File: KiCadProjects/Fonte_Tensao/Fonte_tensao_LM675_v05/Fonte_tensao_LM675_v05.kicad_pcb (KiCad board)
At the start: 2 copper layers, 90 x 100 mm, 33 parts, among them J1 alimentacao analogica, J2 sinais analogicos, J3 comunicacao / sinais digitais, J4 Barrel_Jack, U1 L7809, U2 LM7909_TO220, U3 LM675, U4 L7805, U5 L7905, U6 LM1117T-3.3

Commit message: Roteamento PCB v05
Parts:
- moved C8 95.9 mm to (119.8, 142.2)
- moved C9 87.9 mm to (125.5, 142.2)
- moved U6 76.9 mm to (127.5, 146.8), turned to 180 degrees
- moved U3 75.6 mm to (172.6, 141.6), turned to 180 degrees
- moved C5 74.6 mm to (166.8, 123.5)
- moved SW_kcd1 65.1 mm to (140.3, 83.1)
- moved green1 63.5 mm to (141.3, 145.5)
- moved red1 63.5 mm to (148.8, 145.5)
- moved R1 60.3 mm to (151.5, 122.7), turned to -90 degrees
- moved R2 50.1 mm to (143.8, 117.7), turned to -90 degrees
- moved U5 44.9 mm to (172.4, 55.0)
- moved R6 44.2 mm to (172.7, 111.8), turned to 90 degrees
- moved D1 38.6 mm to (110.9, 67.2)
- moved R7 35.3 mm to (160.0, 115.9), turned to -90 degrees
- moved U2 31.6 mm to (159.9, 55.0)
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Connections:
- J3 pad 16: GND -> Earth
- J3 pad 22: GND -> Earth
- J3 pad 25: GND -> Earth
- J3 pad 28: GND -> Earth
- J3 pad 3: GND -> Earth
- J3 pad 31: GND -> Earth
- J3 pad 34: GND -> Earth
- J3 pad 4: GND -> Earth
- J3 pad 6: GND -> Earth
- J3 pad 7: GND -> Earth
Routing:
- net Earth: track 5.08 -> 437.1 mm
- net VEE: track 0.00 -> 236.0 mm, vias 0 -> 2
- net VCC: track 0.00 -> 174.1 mm
- net +3.3V: track 0.00 -> 104.9 mm
- net Net-(U3-+): track 0.00 -> 94.5 mm
- net -9V: track 0.00 -> 90.0 mm
- net +5V: track 0.00 -> 71.1 mm
- net Net-(U3--): track 0.00 -> 66.6 mm
- net +9V: track 0.00 -> 47.6 mm
- net Net-(green1-A): track 0.00 -> 20.2 mm
- net -5V: track 0.00 -> 18.2 mm
- net Net-(red1-A): track 0.00 -> 15.2 mm
- net Net-(J4-Pad1): track 0.00 -> 12.2 mm
- net Net-(C5-Pad1): track 0.00 -> 6.77 mm
- net GND: track 5.08 -> 0.00 mm
- added copper zone on B.Cu, net Earth

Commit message: placa fonte tensao roteada
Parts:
- moved R6 67.3 mm to (113.2, 143.3)
- moved R5 47.3 mm to (116.2, 123.9), turned to -90 degrees
- moved U3 46.4 mm to (126.2, 141.6)
- moved C9 45.3 mm to (170.8, 142.1)
- moved C8 45.3 mm to (165.0, 142.1)
- moved U6 45.3 mm to (172.8, 146.6)
- moved R1 9.96 mm to (143.8, 116.4)
- moved R2 9.22 mm to (151.5, 122.7)
- moved green1 7.70 mm to (149.0, 145.5)
- moved red1 7.50 mm to (141.3, 145.5)
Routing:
- net Net-(U3--): track 66.6 -> 28.5 mm
- net +3.3V: track 104.9 -> 87.0 mm
- net VEE: track 236.0 -> 252.2 mm, vias 2 -> 1
- net VCC: track 174.1 -> 185.7 mm
- net Earth: track 437.1 -> 447.4 mm
- net Net-(U3-+): track 94.5 -> 84.4 mm
- net Net-(red1-A): track 15.2 -> 21.4 mm
- net Net-(green1-A): track 20.2 -> 15.2 mm
- removed copper zone on B.Cu, net Earth

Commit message: versao para fabricacao jlcpcb revisao Gustavo
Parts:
- removed C6: 1uF, Capacitor_THT:CP_Radial_D5.0mm_P2.50mm
- added C10: 1uF, Capacitor_THT:CP_Radial_Tantal_D4.5mm_P2.50mm, F.Cu at (147.6, 140.3)
- added C11: 2.2uF, Capacitor_THT:CP_Radial_Tantal_D4.5mm_P2.50mm, F.Cu at (128.7, 138.6)
- added C12: 100 nF, Capacitor_THT:C_Disc_D3.0mm_W1.6mm_P2.50mm, F.Cu at (142.1, 140.0)
- C1: value 3.3uF -> 1uF; footprint Capacitor_THT:CP_Radial_D5.0mm_P2.50mm -> Capacitor_THT:CP_Radial_Tantal_D4.5mm_P2.50mm
- C2: value 22uF -> 2.2uF; footprint Capacitor_THT:CP_Radial_D5.0mm_P2.50mm -> Capacitor_THT:CP_Radial_Tantal_D4.5mm_P2.50mm
- C3: value 1uF -> 100 nF; footprint Capacitor_THT:CP_Radial_D5.0mm_P2.50mm -> Capacitor_THT:C_Disc_D3.0mm_W1.6mm_P2.50mm
- C4, C7: footprint Capacitor_THT:CP_Radial_D5.0mm_P2.50mm -> Capacitor_THT:CP_Radial_Tantal_D4.5mm_P2.50mm
- C5: value 2.2uF -> 220nF; footprint Capacitor_THT:CP_Radial_D5.0mm_P2.50mm -> Capacitor_THT:C_Disc_D3.0mm_W1.6mm_P2.50mm
- C8: value 100uF -> 10uF; footprint Capacitor_THT:CP_Radial_D5.0mm_P2.50mm -> Capacitor_THT:CP_Radial_Tantal_D4.5mm_P2.50mm
- C9: value 100uF -> 33uF; footprint Capacitor_THT:CP_Radial_D5.0mm_P2.50mm -> Capacitor_THT:CP_Radial_Tantal_D4.5mm_P2.50mm
- I/0: renamed from SW_kcd1; value chave_gangorra_2_pinos -> Vin
- Vin: renamed from J4; value Barrel_Jack -> Vin
- moved C7 99.5 mm to (119.6, 142.4), turned to -90 degrees
- moved U5 99.0 mm to (131.2, 145.0), turned to 180 degrees
- moved U4 92.5 mm to (148.6, 145.0), turned to 180 degrees
- moved U3 81.9 mm to (111.8, 61.0), turned to 0 degrees
- moved C5 76.2 mm to (115.2, 67.5), turned to 90 degrees
- moved D4 75.7 mm to (128.9, 133.8), turned to 180 degrees
- moved D3 67.6 mm to (140.3, 131.8), turned to 0 degrees
- moved D1 63.4 mm to (173.2, 79.1), turned to 90 degrees
- moved R6 59.6 mm to (111.0, 83.8), turned to 0 degrees
- moved R7 56.5 mm to (117.6, 78.6), turned to 90 degrees
- moved U1 54.9 mm to (169.9, 55.7)
- moved C1 54.8 mm to (169.8, 59.9), turned to -90 degrees
- moved C3 53.6 mm to (176.8, 59.8), turned to -90 degrees
- moved R5 53.2 mm to (111.6, 71.0)
- moved C2 33.7 mm to (126.2, 62.4)
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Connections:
- I/0 pad 1: Net-(J4-Pad1) -> Vin
- R1 pad 1: VCC -> Vin
- Vin pad 1: Net-(J4-Pad1) -> Vin
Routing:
- net Earth: track 447.4 -> 0.00 mm
- net -5V: track 18.2 -> 125.9 mm
- net VEE: track 252.2 -> 166.4 mm, vias 1 -> 0
- net Vin: track 0.00 -> 78.9 mm
- net +9V: track 47.6 -> 109.8 mm
- net Net-(U3-+): track 84.4 -> 31.7 mm
- net +5V: track 71.1 -> 122.0 mm
- net -9V: track 90.0 -> 47.2 mm
- net Net-(U3--): track 28.5 -> 67.4 mm, vias 0 -> 2
- net Net-(red1-A): track 21.4 -> 8.77 mm
- net Net-(J4-Pad1): track 12.2 -> 0.00 mm
- net VCC: track 185.7 -> 194.9 mm
- net Net-(green1-A): track 15.2 -> 8.83 mm
- net Net-(C5-Pad1): track 6.77 -> 4.53 mm
- net +3.3V: track 87.0 -> 85.4 mm
- added copper zone on B.Cu, net Earth
- added copper zone on F.Cu, net Earth
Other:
- board text added: "Fonte tensao V05 2023"
- board text removed: "Barramento EITduino V02"

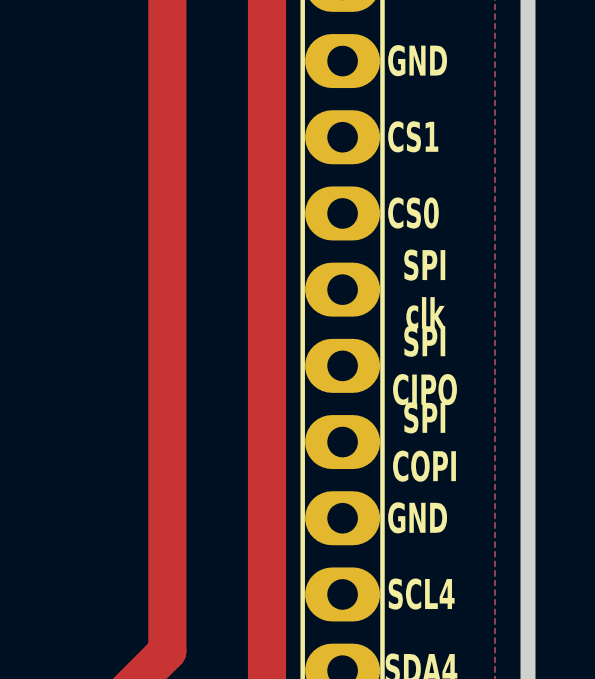
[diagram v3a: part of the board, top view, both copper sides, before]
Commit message: Arquivos Gerber para fabricação de PCB JLCPCB
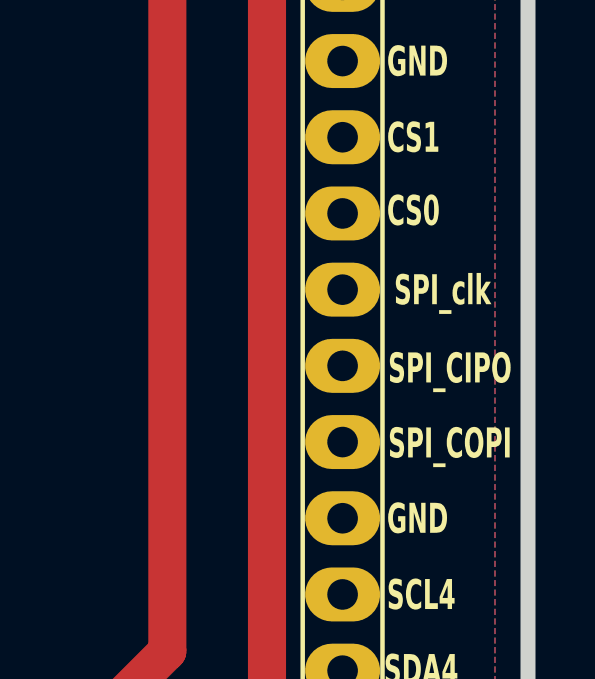
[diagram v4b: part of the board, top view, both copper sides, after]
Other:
- board text added: "SPI_CIPO"
- board text added: "SPI_COPI"
- board text added: "SPI_clk"
- board text removed: "SPI CIPO"
- board text removed: "SPI COPI"
- board text removed: "SPI clk"
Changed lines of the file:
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@@
       (psa4output false)
       (plotreference true)
-      (plotvalue true)
+      (plotvalue false)
       (plotinvisibletext false)
       (sketchpadsonfab false)
@@
     (effects (font (size 1 0.6) (thickness 0.15) bold) (justify left))
   )
-  (gr_text "SPI\nCIPO\n" (at 188.1667 105.432966) (layer "F.SilkS")
+  (gr_text "SPI_CIPO\n" (at 189 105.5) (layer "F.SilkS")
     (effects (font (size 1 0.6) (thickness 0.15) bold))
   )
@@
     (effects (font (size 1 0.6) (thickness 0.15) bold) (justify left))
   )
-  (gr_text "CS0" (at 186.8967 100.352966) (layer "F.SilkS")
+  (gr_text "CS0" (at 186.8967 100.25) (layer "F.SilkS")
     (effects (font (size 1 0.6) (thickness 0.15) bold) (justify left))
   )
@@
     (effects (font (size 1 0.6) (thickness 0.15) bold) (justify left))
   )
-  (gr_text "SPI\nclk\n" (at 188.1667 102.892966) (layer "F.SilkS")
+  (gr_text "SPI_clk\n" (at 188.75 102.892966) (layer "F.SilkS")
     (effects (font (size 1 0.6) (thickness 0.15) bold))
   )
@@
     (effects (font (size 1 0.6) (thickness 0.15) bold) (justify left))
   )
-  (gr_text "SPI\nCOPI\n" (at 188.1667 107.986256) (layer "F.SilkS")
+  (gr_text "SPI_COPI\n" (at 189 108) (layer "F.SilkS")
     (effects (font (size 1 0.6) (thickness 0.15) bold))
   )
